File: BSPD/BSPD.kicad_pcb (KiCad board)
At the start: 2 copper layers, 160 x 124.7 mm, 30 parts, among them J1 DT13-48PABCD-R015, U1 LM317_TO-252, U10 DK1A1B-12V, U2 OP AMP, U3 OP AMP, U4 Inverter (Not Gate), U5 2x4 OR GATE, U6 LM555N, U7 NSL-32, U9 AND GATE

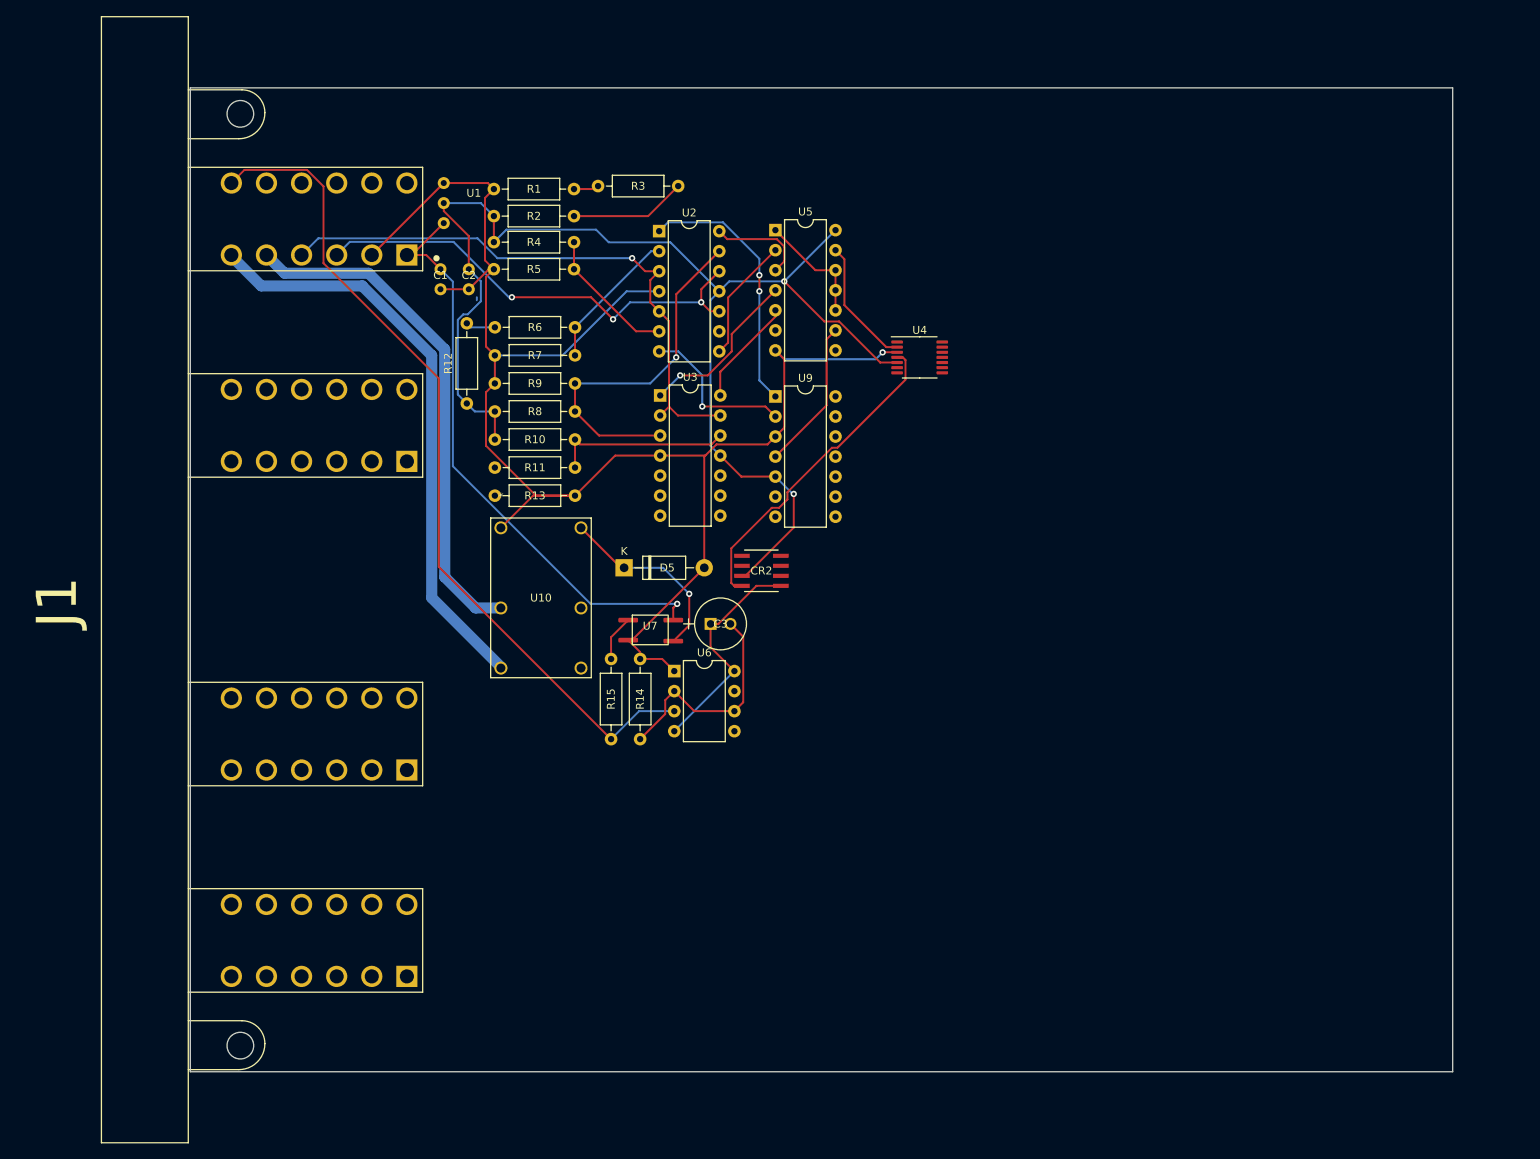
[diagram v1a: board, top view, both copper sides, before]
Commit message: finished shutdown circuitry
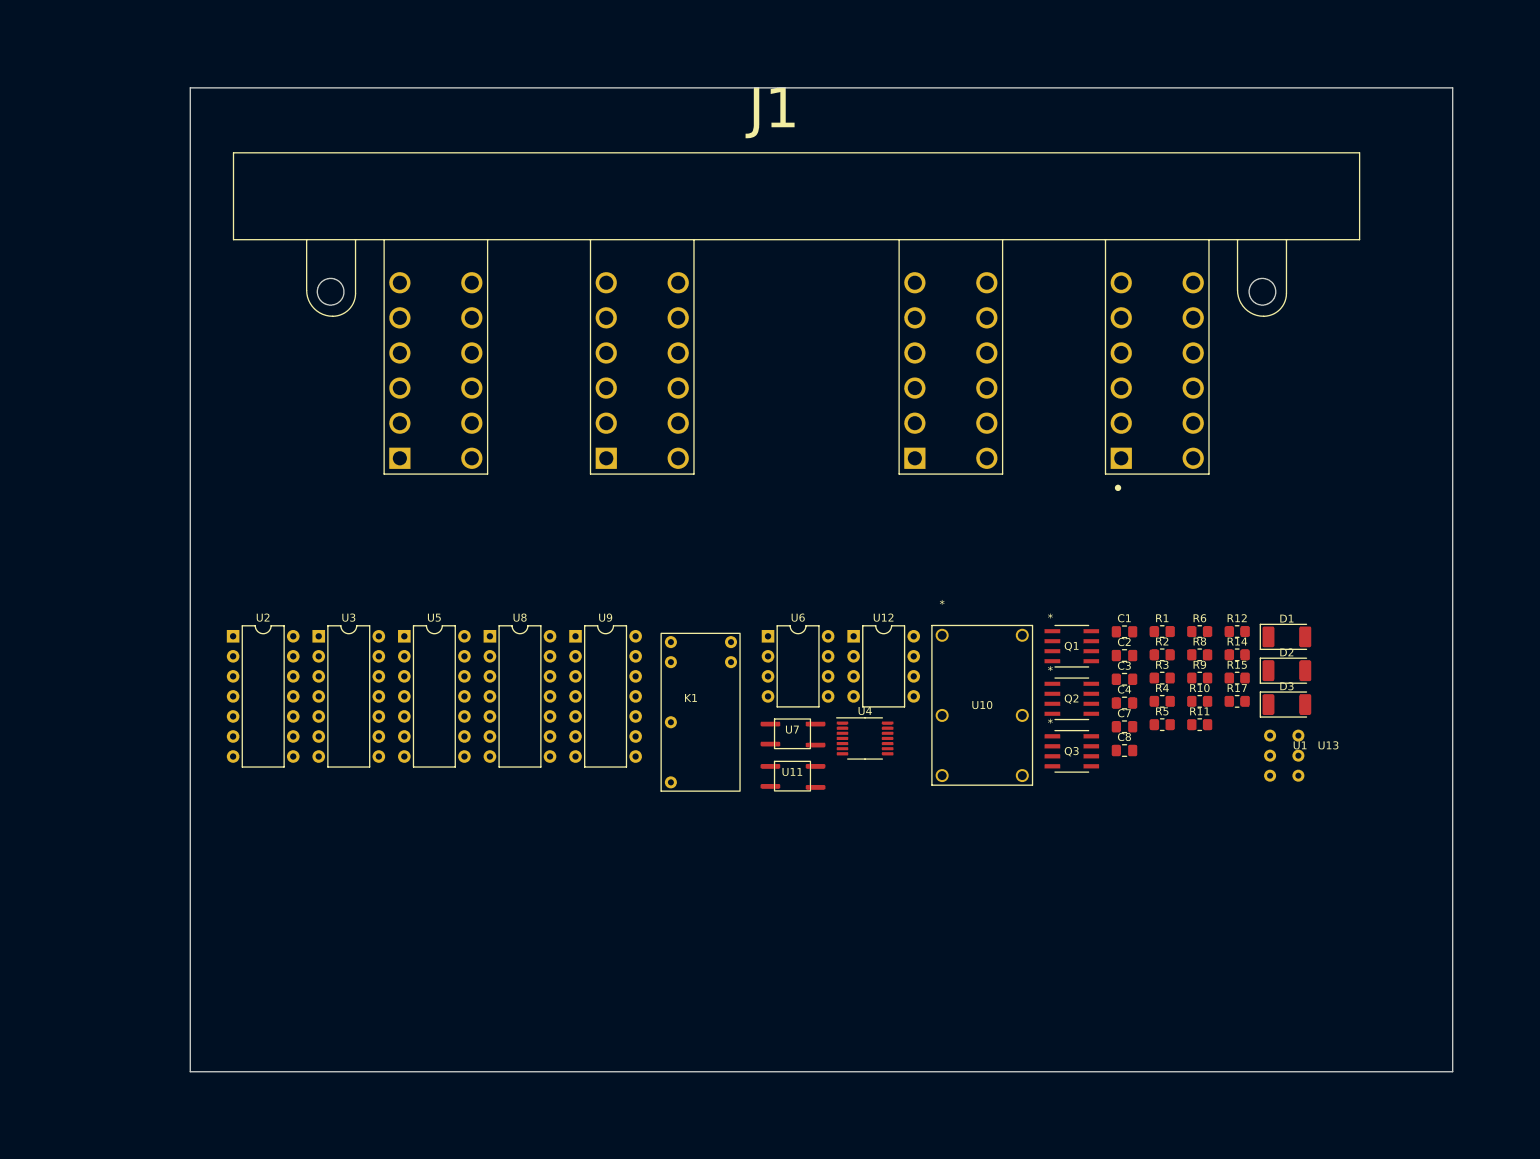
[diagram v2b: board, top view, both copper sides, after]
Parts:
- removed CR2: STS6NF20V, 1FS_2_Global_Footprint_Library:SO-8_STM
- removed D5: D, Diode_THT:D_DO-41_SOD81_P10.16mm_Horizontal
- removed R13: 8.2k, Resistor_THT:R_Axial_DIN0207_L6.3mm_D2.5mm_P10.16mm_Horizontal
- removed R7: 100k, Resistor_THT:R_Axial_DIN0207_L6.3mm_D2.5mm_P10.16mm_Horizontal
- added C4: 1uf, Capacitor_SMD:C_0805_2012Metric_Pad1.18x1.45mm_HandSolder, F.Cu at (144.3, 100.9)
- added C7: 330nf, Capacitor_SMD:C_0805_2012Metric_Pad1.18x1.45mm_HandSolder, F.Cu at (144.3, 103.9)
- added C8: 100nf, Capacitor_SMD:C_0805_2012Metric_Pad1.18x1.45mm_HandSolder, F.Cu at (144.3, 106.9)
- added D1: D, Diode_SMD:D_2010_5025Metric_Pad1.52x2.65mm_HandSolder, F.Cu at (164.9, 92.5)
- added D2: D, Diode_SMD:D_2010_5025Metric_Pad1.52x2.65mm_HandSolder, F.Cu at (164.9, 96.8)
- added D3: D, Diode_SMD:D_2010_5025Metric_Pad1.52x2.65mm_HandSolder, F.Cu at (164.9, 101.1)
- added K1: Latching Relay, 1FS_2_Global_Footprint_Library:Omron G6BK-1114P-US, F.Cu at (89.4, 100.8)
- added Q1: STS6NF20V, 1FS_2_Global_Footprint_Library:SO-8_STM, F.Cu at (137.6, 93.7)
- added Q2: STS6NF20V, 1FS_2_Global_Footprint_Library:SO-8_STM, F.Cu at (137.6, 100.4)
- added Q3: STS6NF20V, 1FS_2_Global_Footprint_Library:SO-8_STM, F.Cu at (137.6, 107.0)
- added R17: 2.4M, Resistor_SMD:R_0805_2012Metric_Pad1.20x1.40mm_HandSolder, F.Cu at (158.6, 100.7)
- added U11: NSL-32, 1FS_2_Global_Footprint_Library:OptoCoupler 6-SOP, F.Cu at (102.2, 110.2)
- added U12: LM555N, Package_DIP:DIP-8_W7.62mm, F.Cu at (110.0, 92.4)
- added U13: LM7805CT, 1FS_2_Global_Footprint_Library:Basic 3 Hole, F.Cu at (166.4, 107.6)
- added U8: NAND, Package_DIP:DIP-14_W7.62mm, F.Cu at (63.9, 92.4)
- C1: value C_Polarized -> 330nf; footprint 1FS_2_Global_Footprint_Library:Basic 2 Hole -> Capacitor_SMD:C_0805_2012Metric_Pad1.18x1.45mm_HandSolder
- C2: value C_Polarized -> 100nf; footprint 1FS_2_Global_Footprint_Library:Basic 2 Hole -> Capacitor_SMD:C_0805_2012Metric_Pad1.18x1.45mm_HandSolder
- C3: value ECA-2DHG010 1uF -> 1uf; footprint 1FS_2_Global_Footprint_Library:PCAP_63x112_PAN -> Capacitor_SMD:C_0805_2012Metric_Pad1.18x1.45mm_HandSolder
- R1: value 20k -> 39k; footprint Resistor_THT:R_Axial_DIN0207_L6.3mm_D2.5mm_P10.16mm_Horizontal -> Resistor_SMD:R_0805_2012Metric_Pad1.20x1.40mm_HandSolder
- R10: value 100k -> 330k; footprint Resistor_THT:R_Axial_DIN0207_L6.3mm_D2.5mm_P10.16mm_Horizontal -> Resistor_SMD:R_0805_2012Metric_Pad1.20x1.40mm_HandSolder
- R11: value 3k -> 39k; footprint Resistor_THT:R_Axial_DIN0207_L6.3mm_D2.5mm_P10.16mm_Horizontal -> Resistor_SMD:R_0805_2012Metric_Pad1.20x1.40mm_HandSolder
- R12: value 22k -> 15k; footprint Resistor_THT:R_Axial_DIN0207_L6.3mm_D2.5mm_P10.16mm_Horizontal -> Resistor_SMD:R_0805_2012Metric_Pad1.20x1.40mm_HandSolder
- R14: footprint Resistor_THT:R_Axial_DIN0207_L6.3mm_D2.5mm_P10.16mm_Horizontal -> Resistor_SMD:R_0805_2012Metric_Pad1.20x1.40mm_HandSolder
- R15: value 480 -> 374; footprint Resistor_THT:R_Axial_DIN0207_L6.3mm_D2.5mm_P10.16mm_Horizontal -> Resistor_SMD:R_0805_2012Metric_Pad1.20x1.40mm_HandSolder
- R2: value 10k -> 18k; footprint Resistor_THT:R_Axial_DIN0207_L6.3mm_D2.5mm_P10.16mm_Horizontal -> Resistor_SMD:R_0805_2012Metric_Pad1.20x1.40mm_HandSolder
- R3: value 47k -> 2.7k; footprint Resistor_THT:R_Axial_DIN0207_L6.3mm_D2.5mm_P10.16mm_Horizontal -> Resistor_SMD:R_0805_2012Metric_Pad1.20x1.40mm_HandSolder
- R4: value 22k -> 18k; footprint Resistor_THT:R_Axial_DIN0207_L6.3mm_D2.5mm_P10.16mm_Horizontal -> Resistor_SMD:R_0805_2012Metric_Pad1.20x1.40mm_HandSolder
- R5: value 100k -> 82k; footprint Resistor_THT:R_Axial_DIN0207_L6.3mm_D2.5mm_P10.16mm_Horizontal -> Resistor_SMD:R_0805_2012Metric_Pad1.20x1.40mm_HandSolder
- R6: value 75k -> 374; footprint Resistor_THT:R_Axial_DIN0207_L6.3mm_D2.5mm_P10.16mm_Horizontal -> Resistor_SMD:R_0805_2012Metric_Pad1.20x1.40mm_HandSolder
- R8: value 11k -> 330k; footprint Resistor_THT:R_Axial_DIN0207_L6.3mm_D2.5mm_P10.16mm_Horizontal -> Resistor_SMD:R_0805_2012Metric_Pad1.20x1.40mm_HandSolder
- R9: value 100k -> 10k; footprint Resistor_THT:R_Axial_DIN0207_L6.3mm_D2.5mm_P10.16mm_Horizontal -> Resistor_SMD:R_0805_2012Metric_Pad1.20x1.40mm_HandSolder
- U1: value LM317_TO-252 -> LM7805CT
- moved U1 126.0 mm to (162.8, 107.6)
- moved R4 102.8 mm to (149.1, 100.7)
- moved R12 101.8 mm to (158.6, 91.8), turned to 0 degrees
- moved R1 101.6 mm to (149.1, 91.8)
- moved C1 97.5 mm to (144.3, 91.9)
- moved R6 97.3 mm to (153.9, 91.8)
- moved C2 95.8 mm to (144.3, 94.9)
- moved R10 95.3 mm to (153.9, 100.7)
- moved R3 94.9 mm to (149.1, 97.7)
- moved R8 94.5 mm to (153.9, 94.8)
- moved R5 94.3 mm to (149.1, 103.6), turned to 0 degrees
- moved R2 93.0 mm to (149.1, 94.8), turned to 0 degrees
- moved R9 87.6 mm to (153.9, 97.7), turned to 0 degrees
- moved R11 85.6 mm to (153.9, 103.6), turned to 0 degrees
- moved R15 79.4 mm to (158.6, 97.7), turned to 0 degrees
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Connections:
- net 0.5V renamed /0.5V
- net 0.68V renamed /0.68V
- net 4.1V renamed /4.1V
- net Brk renamed /Brake Output
- net CrS renamed /Current Output
- J1 pad A10: unconnected-(J1-PadA10) -> /BMS_FAULT 3.3V
- J1 pad A11: unconnected-(J1-PadA11) -> /BMS Light Low Side
- J1 pad A12: unconnected-(J1-PadA12) -> /IMD Light Low Side
- J1 pad A2: GND -> unconnected-(J1-PadA2)
- J1 pad A5: /Shutdown In -> /Current Vref
- J1 pad A6: /Shutdown Out -> /SH_RESET
- J1 pad A7: /BSPD Fault -> unconnected-(J1-PadA7)
- J1 pad A8: unconnected-(J1-PadA8) -> /Shutdown In
- J1 pad A9: unconnected-(J1-PadA9) -> /IMD_FAULT
- J1 pad D1: unconnected-(J1-PadD1) -> GND
- J1 pad D3: unconnected-(J1-PadD3) -> /Shutdown Out
- R1 pad 1: GND -> +5V
- R1 pad 2: Net-(R1-Pad2) -> /4.5V
- R11 pad 2: Net-(R11-Pad2) -> GND
- R12 pad 1: +5V -> GND
- R12 pad 2: Net-(R12-Pad2) -> /3V
- R3 pad 1: Net-(R1-Pad2) -> GND
- R6 pad 1: Net-(R12-Pad2) -> GND
- R6 pad 2: 2.53V -> Net-(U11-K)
- R8 pad 1: +5V -> /4.5V
- R8 pad 2: 4.5V -> GND
- R9 pad 1: 4.5V -> /3V
- R9 pad 2: GND -> +5V
- U10 pad 4: /Shutdown Out -> Net-(K1-Pad4)
- U2 pad 13: 4.5V -> /4.5V
- U2 pad 2: 2.53V -> /Current Vref
- U3 pad 10: unconnected-(U3-Pad10) -> /BMS_FAULT 3.3V
- U3 pad 3: 4.5V -> /4.5V
- U3 pad 8: unconnected-(U3-Pad8) -> /BMS_FAULT 5V
- U3 pad 9: unconnected-(U3-Pad9) -> /3V
- U4 pad 2: Net-(U4-Pad2) -> Net-(U6-Q)
- U4 pad 3: GND -> +5V
- U4 pad 4: Net-(CR2-G) -> /BSPD Fault
- U4 pad 5: +5V -> GND
- U5 pad 13: Net-(U4-Pad2) -> Net-(U6-R)
- U6 pad 3: /BSPD Fault -> Net-(U6-Q)
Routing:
- net GND: track 203.6 -> 0.00 mm, vias 1 -> 0
- net +5V: track 162.7 -> 0.00 mm, vias 2 -> 0
- net /BSPD Fault: track 107.9 -> 0.00 mm
- net /Current Output: track 75.1 -> 0.00 mm, vias 1 -> 0
- net +12V: track 74.9 -> 0.00 mm, vias 1 -> 0
- net /Shutdown Out: track 74.0 -> 0.00 mm
- net /Shutdown In: track 65.2 -> 0.00 mm
- net /Brake Output: track 59.5 -> 0.00 mm, vias 3 -> 0
- net 4.5V: track 45.5 -> 0.00 mm, vias 1 -> 0
- net Net-(CR2-G): track 41.1 -> 0.00 mm
- net Net-(U2-Pad1): track 33.4 -> 0.00 mm, vias 2 -> 0
- net Net-(U6-R): track 28.9 -> 0.00 mm
- net Net-(U6-THR): track 28.7 -> 0.00 mm
- net Net-(D3-K): track 24.0 -> 0.00 mm, vias 1 -> 0
- net /0.5V: track 22.7 -> 0.00 mm
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
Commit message: 1/2 BSPD Circuitry
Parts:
- removed C7: 330nf, Capacitor_SMD:C_0805_2012Metric_Pad1.18x1.45mm_HandSolder
- removed C8: 100nf, Capacitor_SMD:C_0805_2012Metric_Pad1.18x1.45mm_HandSolder
- removed Q1: STS6NF20V, 1FS_2_Global_Footprint_Library:SO-8_STM
- removed R2: 18k, Resistor_SMD:R_0805_2012Metric_Pad1.20x1.40mm_HandSolder
- removed R3: 2.7k, Resistor_SMD:R_0805_2012Metric_Pad1.20x1.40mm_HandSolder
- removed U13: LM7805CT, 1FS_2_Global_Footprint_Library:Basic 3 Hole
- added C10: 0.33µF, Capacitor_SMD:C_0805_2012Metric_Pad1.18x1.45mm_HandSolder, F.Cu at (77.6, 109.2)
- added C11: 100nf, Capacitor_SMD:C_0805_2012Metric_Pad1.18x1.45mm_HandSolder, F.Cu at (88.0, 32.4)
- added C12: 100nf, Capacitor_SMD:C_0805_2012Metric_Pad1.18x1.45mm_HandSolder, F.Cu at (87.6, 57.2)
- added C13: 100nf, Capacitor_SMD:C_0805_2012Metric_Pad1.18x1.45mm_HandSolder, F.Cu at (101.2, 55.0)
- added C14: 100nf, Capacitor_SMD:C_0805_2012Metric_Pad1.18x1.45mm_HandSolder, F.Cu at (88.4, 41.8)
- added C15: 100nf, Capacitor_SMD:C_0805_2012Metric_Pad1.18x1.45mm_HandSolder, F.Cu at (101.5, 68.7)
- added C16: 100nf, Capacitor_SMD:C_0805_2012Metric_Pad1.18x1.45mm_HandSolder, F.Cu at (114.9, 71.1)
- added C5: 100nF, Capacitor_SMD:C_0805_2012Metric_Pad1.18x1.45mm_HandSolder, F.Cu at (74.2, 123.2)
- added C6: 100nF, Capacitor_SMD:C_0805_2012Metric_Pad1.18x1.45mm_HandSolder, F.Cu at (74.0, 119.9)
- added C9: 0.33µF, Capacitor_SMD:C_0805_2012Metric_Pad1.18x1.45mm_HandSolder, F.Cu at (77.6, 106.2)
- added R13: 39k, Resistor_SMD:R_0805_2012Metric_Pad1.20x1.40mm_HandSolder, F.Cu at (68.6, 52.7)
- added R16: 39k, Resistor_SMD:R_0805_2012Metric_Pad1.20x1.40mm_HandSolder, F.Cu at (68.5, 55.9)
- added R18: 1M, Resistor_SMD:R_0805_2012Metric_Pad1.20x1.40mm_HandSolder, F.Cu at (72.6, 55.9)
- added R19: 22k 1%, Resistor_SMD:R_0805_2012Metric_Pad1.20x1.40mm_HandSolder, F.Cu at (69.4, 47.8)
- added R20: 18k 1%, Resistor_SMD:R_0805_2012Metric_Pad1.20x1.40mm_HandSolder, F.Cu at (69.4, 49.9)
- added R7: 120, Resistor_SMD:R_0805_2012Metric_Pad1.20x1.40mm_HandSolder, F.Cu at (73.8, 116.4)
- added U14: ISO1050DUB, Package_SO:SOP-8_6.62x9.15mm_P2.54mm, F.Cu at (64.6, 130.9)
- added U15: LM7809_TO220, Package_TO_SOT_THT:TO-220-3_Vertical, F.Cu at (70.9, 105.4)
- C4: value 1uf -> 100nf
- R17: value 2.4M -> 1M
- U1: footprint 1FS_2_Global_Footprint_Library:Basic 3 Hole -> Package_TO_SOT_THT:TO-220-3_Vertical
- U12: value LM555N -> OP AMP; footprint Package_DIP:DIP-8_W7.62mm -> Package_DIP:DIP-14_W7.62mm
- U4: value Inverter (Not Gate) -> NUCLEO-L432KC; footprint Package_SO:TSSOP-14_4.4x5mm_P0.65mm -> 1FS_2_Global_Footprint_Library:MODULE_NUCLEO-L432KC
- moved U1 123.6 mm to (62.4, 35.4), turned to -90 degrees
- moved R8 108.8 mm to (69.4, 26.2), turned to 180 degrees
- moved R9 105.4 mm to (69.3, 34.8), turned to 180 degrees
- moved R12 104.8 mm to (69.3, 37.0)
- moved C1 103.7 mm to (58.5, 33.7)
- moved C2 103.7 mm to (58.5, 36.7)
- moved R11 102.5 mm to (69.4, 45.6), turned to 180 degrees
- moved R10 102.1 mm to (69.3, 43.4)
- moved R1 102.0 mm to (69.3, 28.3)
- moved R5 101.3 mm to (69.3, 41.3), turned to 180 degrees
- moved R4 100.8 mm to (69.3, 39.1)
- moved D3 99.6 mm to (73.8, 60.9), turned to 90 degrees
- moved R17 98.6 mm to (72.5, 52.7), turned to 180 degrees
- moved D1 94.3 mm to (73.7, 68.6), turned to 90 degrees
- moved D2 93.8 mm to (73.5, 75.6), turned to 90 degrees
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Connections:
- net /4.1V renamed /Brake Threshhold (4.1V)
- net Net-(U2-Pad14) renamed /BrkSenShort
- net Net-(U2-Pad8) renamed /BrkSenOpen
- net Net-(U3-Pad1) renamed /CurSenShort
- net Net-(U3-Pad14) renamed /CurSenOpen
- C3 pad 1: Net-(U6-R) -> /BSPD Fault
- C4 pad 1: +5V -> GND
- C4 pad 2: Net-(U12-THR) -> +5V
- D1 pad 2: Net-(D1-A) -> GND
- J1 pad A10: /BMS_FAULT 3.3V -> unconnected-(J1-PadA10)
- J1 pad A11: /BMS Light Low Side -> unconnected-(J1-PadA11)
- J1 pad A12: /IMD Light Low Side -> unconnected-(J1-PadA12)
- J1 pad A2: unconnected-(J1-PadA2) -> /Shutdown In
- J1 pad A6: /SH_RESET -> unconnected-(J1-PadA6)
- J1 pad A8: /Shutdown In -> unconnected-(J1-PadA8)
- J1 pad A9: /IMD_FAULT -> unconnected-(J1-PadA9)
- J1 pad B1: unconnected-(J1-PadB1) -> /CAN_Tel_H
- J1 pad B12: unconnected-(J1-PadB12) -> /CAN_Tel_L
- J1 pad D10: unconnected-(J1-PadD10) -> /BMS Light Low Side
- J1 pad D11: unconnected-(J1-PadD11) -> /IMD Light Low Side
- J1 pad D12: unconnected-(J1-PadD12) -> /Shutdown Out
- J1 pad D3: /Shutdown Out -> unconnected-(J1-PadD3)
- J1 pad D7: unconnected-(J1-PadD7) -> /SH_RESET
- J1 pad D8: unconnected-(J1-PadD8) -> /IMD_FAULT 5V
- J1 pad D9: unconnected-(J1-PadD9) -> /BMS_FAULT 5V
- K1 pad 2: Net-(D1-A) -> GND
- R15 pad 2: /BSPD Fault -> /BSPD Fault Post Timer
- R17 pad 1: Net-(U12-THR) -> /Current Sensor Differential
- R17 pad 2: GND -> /Current Vref Op
- U11 pad 1: Net-(U11-A) -> /BSPD Fault Post Timer
- U12 pad 1: GND -> /Current Vref Buffered
- U12 pad 2: Net-(U12-THR) -> /Current Vref Buffered
- U12 pad 3: /IMD Latch Delay -> /Current Vref
- U12 pad 4: +5V -> GND
- U12 pad 6: Net-(U12-THR) -> unconnected-(U12-Pad6)
- U12 pad 8: +5V -> unconnected-(U12-Pad8)
- U2 pad 2: /Current Vref -> /2.25V
- U2 pad 3: /Current Output -> /Current Sensor Differential
- U2 pad 5: /Current Output -> /Brake Output
- U3 pad 10: /BMS_FAULT 3.3V -> /Current Output
- U3 pad 5: unconnected-(U3-Pad5) -> /Current Vref Op
- U3 pad 6: unconnected-(U3-Pad6) -> /Current Output Op
- U3 pad 7: unconnected-(U3-Pad7) -> /Current Sensor Differential
- U3 pad 8: /BMS_FAULT 5V -> /Current Output Buffered
- U3 pad 9: /3V -> /Current Output Buffered
- U5 pad 13: Net-(U6-R) -> /BSPD Fault
- U6 pad 4: Net-(U6-R) -> /BSPD Fault
- U6 pad 8: Net-(U6-R) -> +5V
- U8 pad 1: /BSPD_FAULT -> Net-(U6-Q)
- U8 pad 14: (no net) -> +5V
- U8 pad 2: /IMD_FAULT 5V -> Net-(U6-Q)
- U8 pad 7: (no net) -> GND
- U8 pad 8: /BMS_FAULT 5V -> Net-(U6-Q)
- U8 pad 9: Net-(U11-A) -> /BSPD Fault Post Timer
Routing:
- net GND: track 0.00 -> 355.1 mm, vias 0 -> 5
- net +5V: track 0.00 -> 177.4 mm, vias 0 -> 5
- net +12V: track 0.00 -> 112.0 mm
- net /SH_RESET: track 0.00 -> 61.9 mm, vias 0 -> 1
- net /Current Vref: track 0.00 -> 55.7 mm
- net /Brake Output: track 0.00 -> 53.3 mm
- net /Current Output: track 0.00 -> 51.1 mm, vias 0 -> 2
- net /4.5V: track 0.00 -> 43.9 mm
- net /BSPD Fault Post Timer: track 0.00 -> 36.6 mm
- net /BSPD Fault: track 0.00 -> 35.4 mm, vias 0 -> 1
- net /BrkSenShort: track 0.00 -> 32.7 mm, vias 0 -> 1
- net Net-(U6-Q): track 0.00 -> 29.9 mm
- net Net-(U5-Pad9): track 0.00 -> 28.9 mm
- net /Shutdown In: track 0.00 -> 28.7 mm
- net Net-(D1-K): track 0.00 -> 27.6 mm
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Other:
- board size 160 x 124.7 mm -> 167.9 x 124.7 mm

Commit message: finished board layout
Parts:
- moved R7 19.5 mm to (60.6, 130.8), turned to -90 degrees
- moved C5 12.4 mm to (62.4, 127.0), turned to -90 degrees
- moved U14 5.27 mm to (69.8, 130.9)
- moved C6 4.39 mm to (75.7, 124.0)
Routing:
- net GND: track 355.1 -> 469.1 mm, vias 5 -> 8
- net +5V: track 177.4 -> 257.4 mm, vias 5 -> 7
- net +9V: track 6.13 -> 65.5 mm, vias 0 -> 1
- net /BMS_FAULT 5V: track 0.00 -> 58.1 mm, vias 0 -> 2
- net /IMD_FAULT 5V: track 0.00 -> 52.9 mm, vias 0 -> 2
- net /BMS Light Low Side: track 0.00 -> 51.7 mm, vias 0 -> 4
- net /IMD Light Low Side: track 0.00 -> 45.7 mm, vias 0 -> 1
- net /CAN1_TD: track 0.00 -> 38.3 mm
- net +3.3V: track 0.00 -> 25.0 mm, vias 0 -> 2
- net /CAN1_RD: track 0.00 -> 18.1 mm
- net +12V: track 112.0 -> 104.8 mm
- net /CAN_Tel_H: track 7.29 -> 12.6 mm
- net /CAN_Tel_L: track 7.29 -> 12.6 mm
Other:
- board text added: "100nf"
- board text added: "555 TIMER"

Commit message: Silk screen complete
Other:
- board text added: "10k Ω"
- board text added: "15k Ω"
- board text added: "18k Ω"
- board text added: "18k Ω 1%"
- board text added: "1M Ω"
- board text added: "1uf"
- board text added: "22k Ω 1%"
- board text added: "270k Ω"
- board text added: "2x4 OR"
- board text added: "330k Ω"
- board text added: "330nf"
- board text added: "370 Ω"
- board text added: "39k Ω"
- board text added: "3x3 NAND"
- board text added: "4x2 OR"
- board text added: "5V lin reg"
- board text added: "82k Ω"
- board text added: "9V lin reg"
- board text added: "BSPD Latching Relay"
- board text added: "BSPD NO Relay"
- board text added: "CAN Termination 120 Ω"
- board text added: "CAN Transceiver"
- board text added: "N-channel Mosfet"
- board text added: "Nucleo L432KC"
- board text added: "Op Amp"
- board text added: "Optocoupler"
- board text added: "Relay coil breakdown diode"
